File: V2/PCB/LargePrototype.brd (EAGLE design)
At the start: 100 x 100 mm, 231 parts, among them U1 GENERIC-SOIC8, U2 GENERIC-SOIC8, U3 GENERIC-SOIC8, U4 GENERIC-SOIC8

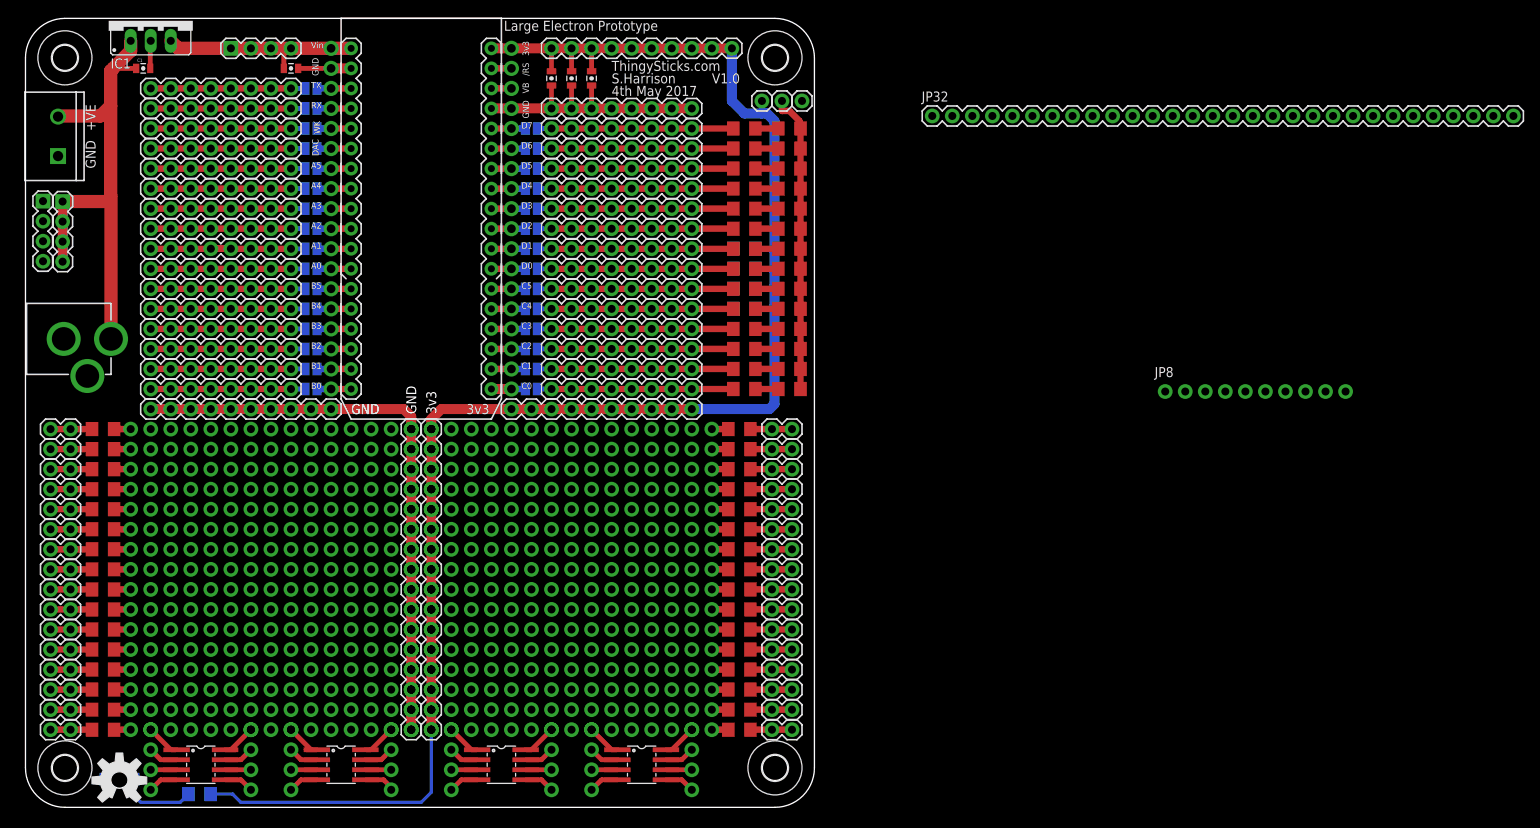
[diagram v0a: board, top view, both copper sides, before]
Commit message: Minor fixes for location of silk screen.
Added pdf's and images of pcb/schematic.

Added to DirtyPCBs order.
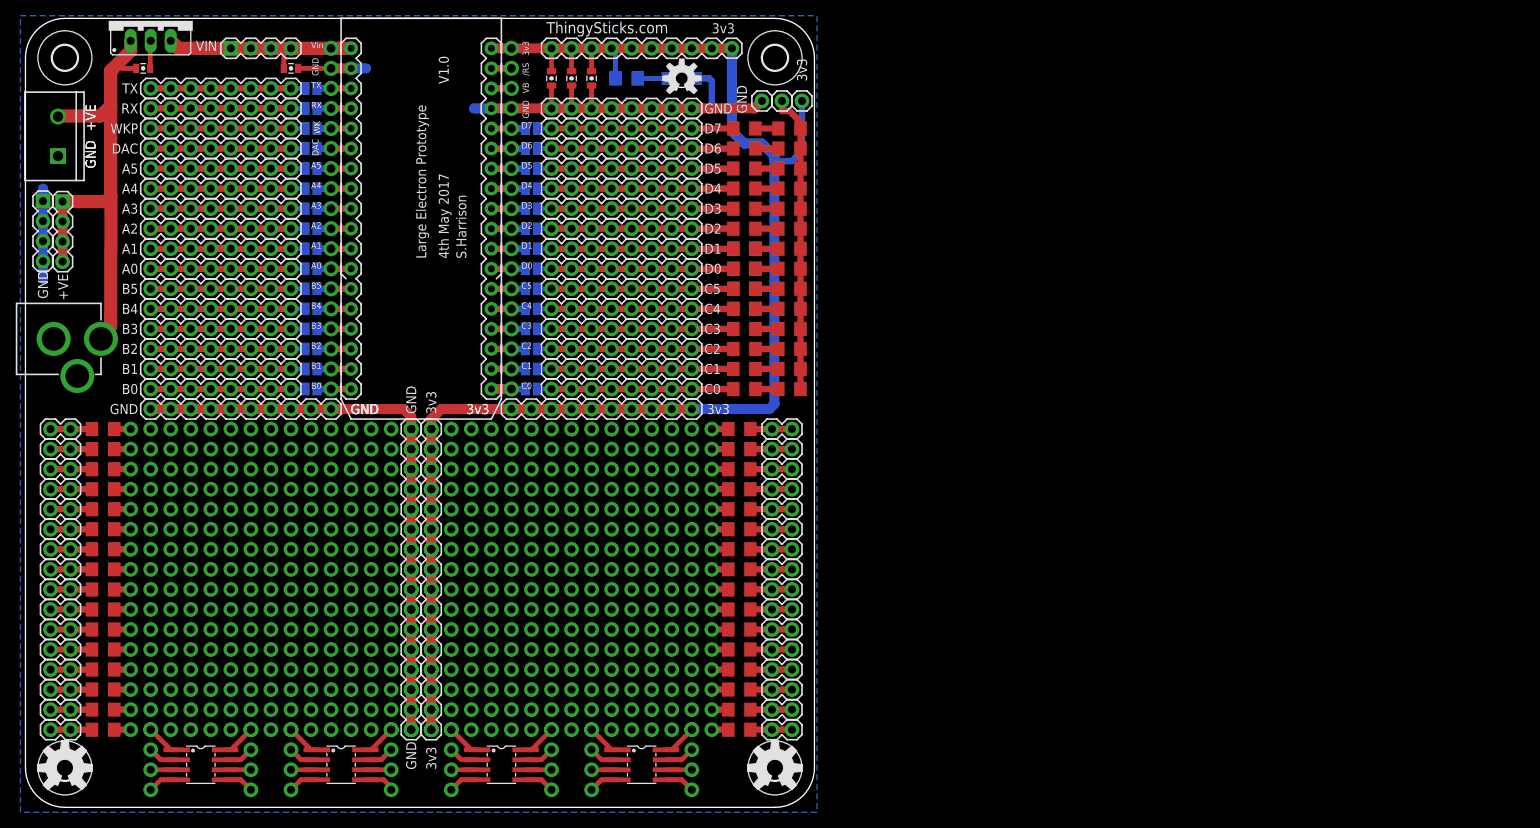
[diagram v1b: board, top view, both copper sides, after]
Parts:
- removed JP32: Alignment, SparkFun-Connectors:1X30
- removed JP8: Alignment, SparkFun-Connectors:1X10_NO_SILK
- added LOGO2: OSHW-LOGOL, SparkFun-Aesthetics:OSHW-LOGO-L
- added LOGO3: OSHW-LOGOM, SparkFun-Aesthetics:OSHW-LOGO-M
- JP16: value 3v3 -> (none)
- JP33: value GND -> (none)
- moved D1 113.9 mm to (83.2, 92.4), turned to 180 degrees
- moved R1 105.6 mm to (76.2, 92.4), turned to 0 degrees
- moved LOGO1 7.08 mm to (5.00, 5.00)
- moved JP16 5.08 mm to (98.4, 89.5)
- moved JP33 5.08 mm to (93.3, 89.5)
- moved JP110 1.27 mm to (-4.13, 59.4)
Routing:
- net GND: track 117.5 -> 188.6 mm
- net 3.3V: track 243.3 -> 257.0 mm
- net N$94: track 7.62 -> 0.00 mm
- net N$1: track 9.80 -> 3.79 mm
- net 12V: track 63.0 -> 63.5 mm
- added copper zone on layer 16, net GND

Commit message: Relabelled large electron prototype as V2 to match the folder.
Improved silk screen

Removed jumper links for electron pins so they are connected through

Added a couple more capacitor places.

Added 3v3 and GND links to lower half board edge
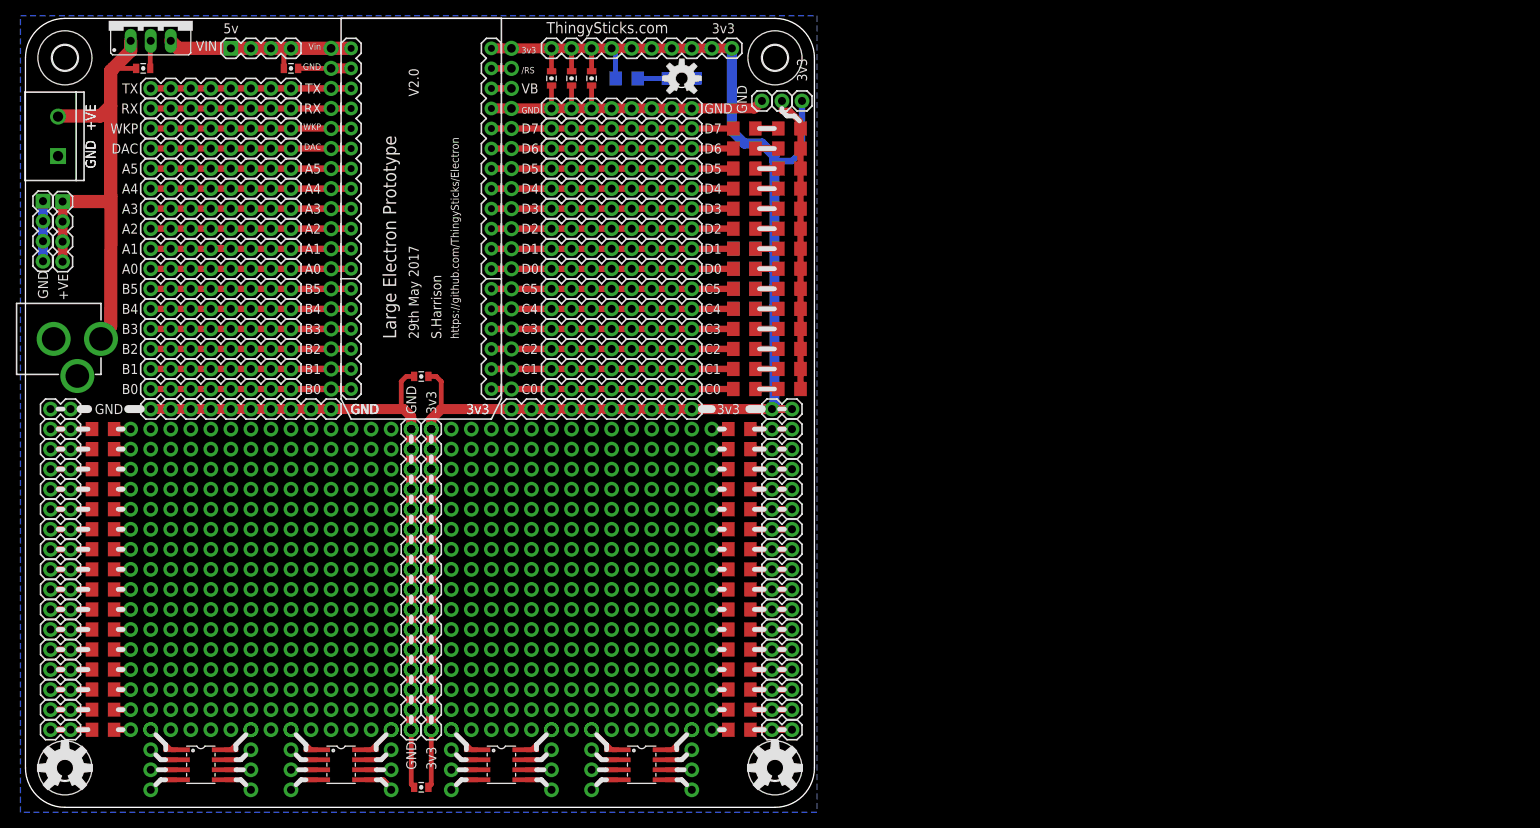
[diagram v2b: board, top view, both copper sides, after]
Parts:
- removed SJ1, SJ10, SJ11, SJ12, SJ13, SJ14, SJ15, SJ16, SJ17, SJ18, SJ19, SJ2, SJ20, SJ21, SJ22, SJ23, SJ24, SJ25, SJ26, SJ27, SJ28, SJ29, SJ3, SJ30, SJ4, SJ5, SJ6, SJ7, SJ8, SJ9: (no value), jumper:SJ
- added C6, C7: (no value), SparkFun-Capacitors:0805-CAP
- added JP32, JP8: (no value), SparkFun-Connectors:1X02
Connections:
- removed net C4: SJ6.1, U$1.C4, U$1.C4_1
- removed net C5: SJ7.1, U$1.C5, U$1.C5_1
- removed net D0: SJ30.1, U$1.D0, U$1.D0_1
- removed net D1: SJ29.1, U$1.D1, U$1.D1_1
- removed net N$100: SJ4.1, U$1.C2, U$1.C2_1
- removed net N$101: SJ3.1, U$1.C1, U$1.C1_1
- removed net N$102: SJ2.1, U$1.C0, U$1.C0_1
- removed net N$103: SJ8.1, U$1.D2, U$1.D2_1
- removed net N$105: SJ9.1, U$1.D3, U$1.D3_1
- removed net N$106: SJ11.1, U$1.D4, U$1.D4_1
- removed net N$107: SJ10.1, U$1.D5, U$1.D5_1
- removed net N$108: SJ12.1, U$1.D6, U$1.D6_1
- removed net N$109: SJ13.1, U$1.D7, U$1.D7_1
- removed net N$112: SJ14.2, U$1.TX, U$1.TX_1
- removed net N$113: SJ15.2, U$1.RX, U$1.RX_1
- removed net N$114: SJ16.2, U$1.WKP, U$1.WKP_1
- removed net N$115: SJ17.2, U$1.DAC, U$1.DAC_1
- removed net N$116: SJ18.2, U$1.A5, U$1.A5_1
- removed net N$117: SJ19.2, U$1.A4, U$1.A4_1
- removed net N$118: SJ20.2, U$1.A3, U$1.A3_1
- removed net N$119: SJ21.2, U$1.A2, U$1.A2_1
- removed net N$120: SJ22.2, U$1.A1, U$1.A1_1
- removed net N$121: SJ23.2, U$1.A0, U$1.A0_1
- removed net N$122: SJ24.2, U$1.B5, U$1.B5_1
- removed net N$123: SJ25.2, U$1.B4, U$1.B4_1
- removed net N$124: SJ26.2, U$1.B3, U$1.B3_1
- removed net N$125: SJ27.2, U$1.B2, U$1.B2_1
- removed net N$126: SJ28.2, U$1.B1, U$1.B1_1
- removed net N$127: SJ1.2, U$1.B0, U$1.B0_1
- removed net N$99: SJ5.1, U$1.C3, U$1.C3_1
- net 3.3V: now also C6.1, C7.1, JP8.1, JP8.2
- net A0C: now also U$1.A0, U$1.A0_1; no longer SJ23.1
- net A1C: now also U$1.A1, U$1.A1_1; no longer SJ22.1
- net A2C: now also U$1.A2, U$1.A2_1; no longer SJ21.1
- net A3C: now also U$1.A3, U$1.A3_1; no longer SJ20.1
- net A4C: now also U$1.A4, U$1.A4_1; no longer SJ19.1
- net A5C: now also U$1.A5, U$1.A5_1; no longer SJ18.1
- net B0C: now also U$1.B0, U$1.B0_1; no longer SJ1.1
- net B1C: now also U$1.B1, U$1.B1_1; no longer SJ28.1
- net B2C: now also U$1.B2, U$1.B2_1; no longer SJ27.1
- net B3C: now also U$1.B3, U$1.B3_1; no longer SJ26.1
- net B4C: now also U$1.B4, U$1.B4_1; no longer SJ25.1
- net B5C: now also U$1.B5, U$1.B5_1; no longer SJ24.1
- net C0C: now also U$1.C0, U$1.C0_1; no longer SJ2.2
- net C1C: now also U$1.C1, U$1.C1_1; no longer SJ3.2
- net C2C: now also U$1.C2, U$1.C2_1; no longer SJ4.2
- net C3C: now also U$1.C3, U$1.C3_1; no longer SJ5.2
- net C4C: now also U$1.C4, U$1.C4_1; no longer SJ6.2
- net C5C: now also U$1.C5, U$1.C5_1; no longer SJ7.2
- net D0C: now also U$1.D0, U$1.D0_1; no longer SJ30.2
- net D1C: now also U$1.D1, U$1.D1_1; no longer SJ29.2
- net D2C: now also U$1.D2, U$1.D2_1; no longer SJ8.2
- net D3C: now also U$1.D3, U$1.D3_1; no longer SJ9.2
- net D4C: now also U$1.D4, U$1.D4_1; no longer SJ11.2
- net D5C: now also U$1.D5, U$1.D5_1; no longer SJ10.2
- net D6C: now also U$1.D6, U$1.D6_1; no longer SJ12.2
- net D7C: now also U$1.D7, U$1.D7_1; no longer SJ13.2
- net DACC: now also U$1.DAC, U$1.DAC_1; no longer SJ17.1
- net GND: now also C6.2, C7.2, JP32.1, JP32.2
- net RXC: now also U$1.RX, U$1.RX_1; no longer SJ15.1
- net TXC: now also U$1.TX, U$1.TX_1; no longer SJ14.1
- net WKPC: now also U$1.WKP, U$1.WKP_1; no longer SJ16.1
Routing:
- net 3.3V: track 257.0 -> 283.1 mm
- net D7C: track 24.8 -> 30.7 mm
- net D6C: track 24.8 -> 30.7 mm
- net D5C: track 24.8 -> 30.7 mm
- net D4C: track 24.8 -> 30.7 mm
- net D3C: track 24.8 -> 30.7 mm
- net D2C: track 24.8 -> 30.7 mm
- net D1C: track 30.1 -> 35.9 mm
- net D0C: track 30.1 -> 35.9 mm
- net C5C: track 30.1 -> 35.9 mm
- net C4C: track 30.1 -> 35.9 mm
- net C3C: track 24.8 -> 30.7 mm
- net C2C: track 24.8 -> 30.7 mm
- net C1C: track 24.8 -> 30.7 mm
- net C0C: track 24.8 -> 30.7 mm
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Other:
- board text added: "29th May 2017"
- board text added: "5v"
- board text added: "A6"
- board text added: "RST"
- board text added: "V2.0"
- board text added: "VBATT"
- board text added: "https://github.com/ThingySticks/Electron"
- board text removed: "4th May 2017"
- board text removed: "V1.0"

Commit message: Renamed electron & added pictures.
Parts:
- renumbered U$1 to IC2
